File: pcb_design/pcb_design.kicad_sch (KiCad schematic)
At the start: 8 parts, among them J1 USB_C_Receptacle_USB2.0_16P, U1 AP2112K-3.3, U2 ESP32-C3-WROOM-02

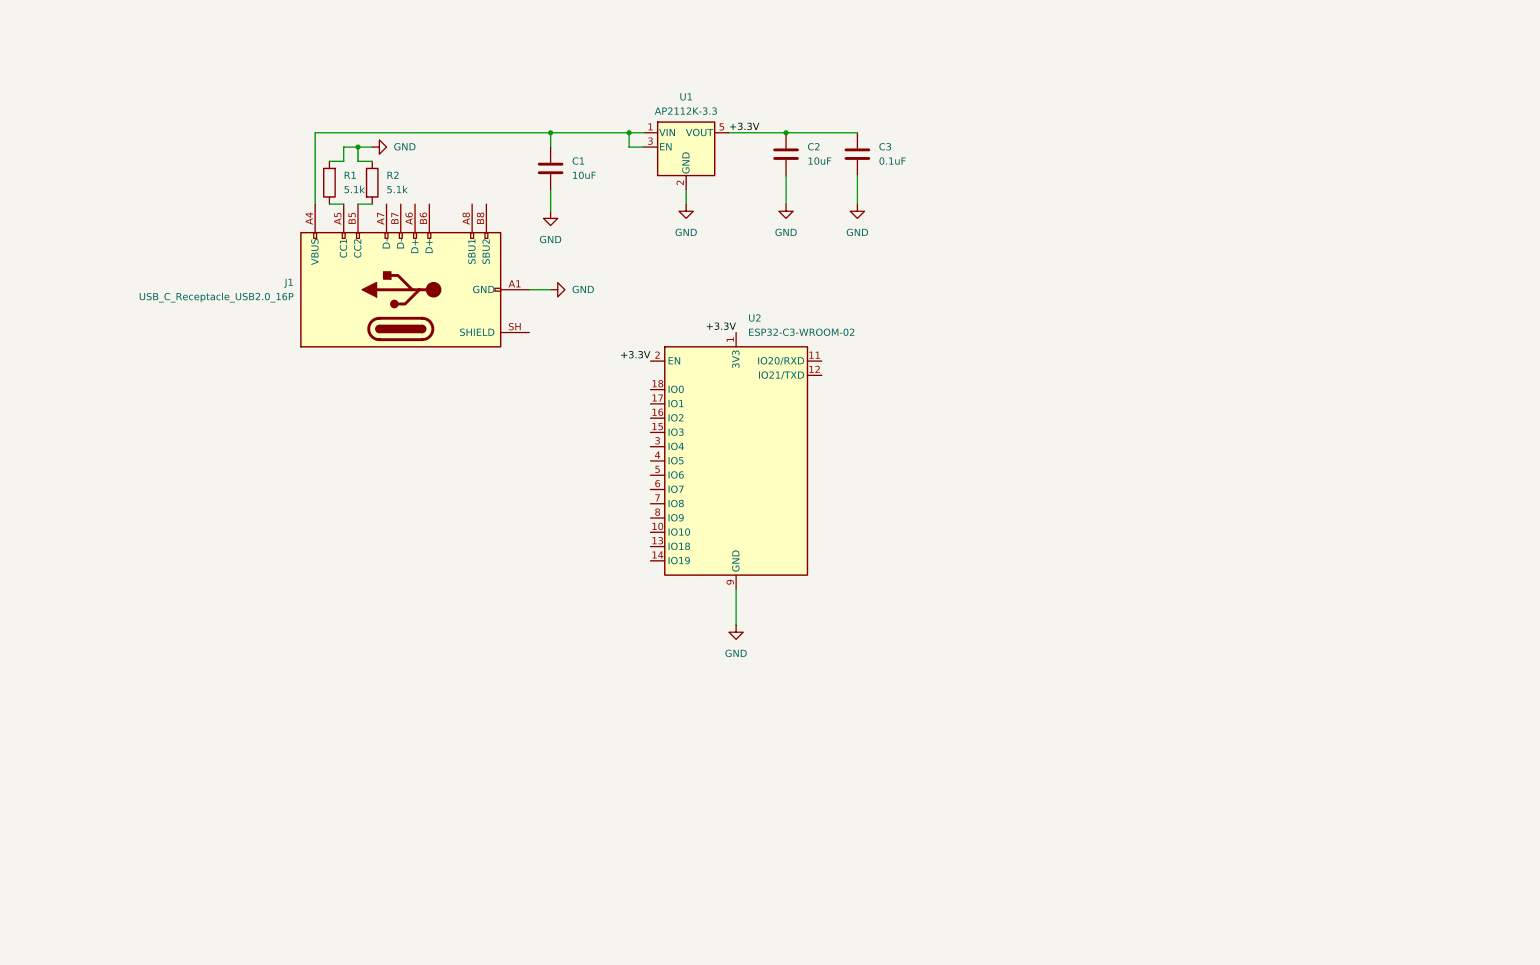
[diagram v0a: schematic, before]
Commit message: feat: completar esquema electronico de la pulsera con magnetometro real y carga LiPo
- Reemplaza el conector generico del QMC6308 por su simbolo/footprint real
  (WLCSP-4, libreria propia en pcb_design/libs) para ensamblaje SMT en JLCPCB
- Agrega regulador de 1.8V (AP2112K-1.8) y level shifter I2C (TXS0102DCU),
  porque el QMC6308 no soporta el bus de 3.3V ya existente
- Agrega circuito de carga LiPo (MCP73831) alimentado desde el mismo USB-C,
  con conector JST-PH para la bateria
- Reemplaza los transistores de simulacion por MMBT3904 reales y asigna
  footprint a todos los componentes (incluido el USB-C: HRO TYPE-C-31-M-12)
- Corrige la alimentacion del ESP32, los pull-ups I2C faltantes y la
  conexion CC1/CC2 del USB-C

Estructura de componentes, conexiones y revision asistida por Claude,
validado con ERC (0 errores) y verificacion de netlist en cada paso.

Co-Authored-By: Claude Sonnet 5 <noreply@anthropic.com>
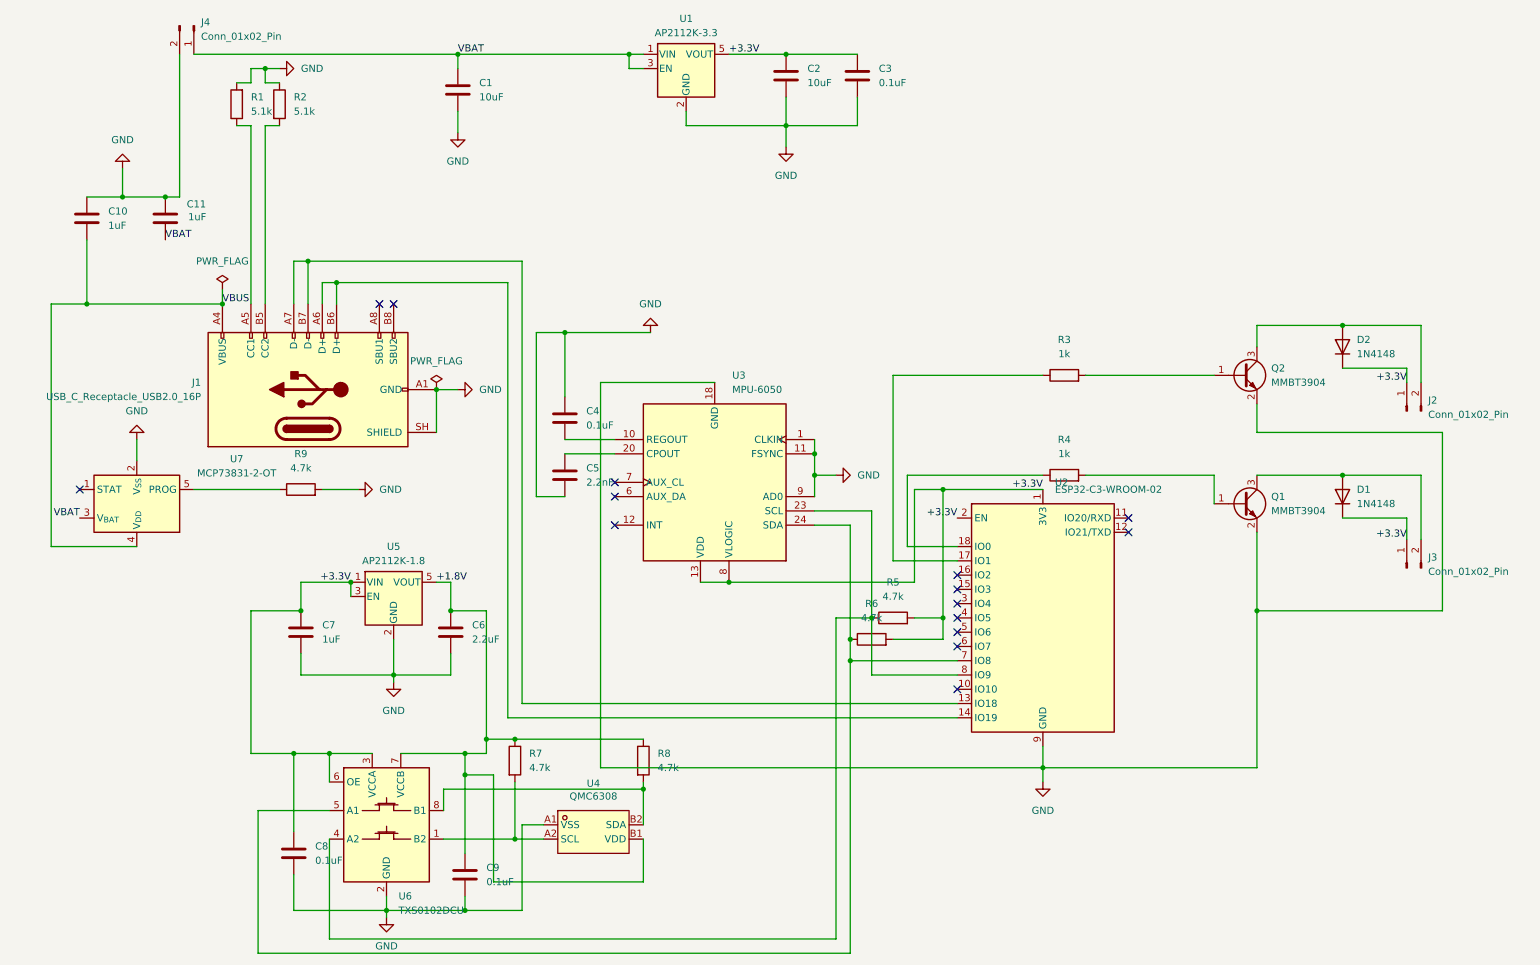
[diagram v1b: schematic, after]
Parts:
- added C10, C11: 1uF, Capacitor_SMD:C_0805_2012Metric, symbol Device:C
- added C4, C8, C9: 0.1uF, Capacitor_SMD:C_0603_1608Metric, symbol Device:C
- added C5: 2.2nF, Capacitor_SMD:C_0603_1608Metric, symbol Device:C
- added C6: 2.2uF, Capacitor_SMD:C_0805_2012Metric, symbol Device:C
- added C7: 1uF, Capacitor_SMD:C_0603_1608Metric, symbol Device:C
- added D1, D2: 1N4148, Diode_THT:D_DO-35_SOD27_P7.62mm_Horizontal, symbol Diode:1N4148
- added J2, J3: Conn_01x02_Pin, Connector_PinHeader_2.54mm:PinHeader_1x02_P2.54mm_Vertical, symbol Connector:Conn_01x02_Pin
- added J4: Conn_01x02_Pin, symbol Connector:Conn_01x02_Pin
- added Q1, Q2: MMBT3904, Package_TO_SOT_SMD:SOT-23, symbol Transistor_BJT:MMBT3904
- added R3, R4: 1k, Resistor_SMD:R_0603_1608Metric, symbol Device:R
- added R5, R6, R7, R8, R9: 4.7k, Resistor_SMD:R_0603_1608Metric, symbol Device:R
- added U3: MPU-6050, Sensor_Motion:InvenSense_QFN-24_4x4mm_P0.5mm, symbol Sensor_Motion:MPU-6050
- added U4: QMC6308, ACPI_QMC6308:WLCSP-4_L0.8-W0.8-R2-C2-P0.40-BL, symbol ACPI_QMC6308:QMC6308
- added U5: AP2112K-1.8, Package_TO_SOT_SMD:SOT-23-5, symbol Regulator_Linear:AP2112K-1.8
- added U6: TXS0102DCU, Package_SO:VSSOP-8_2.3x2mm_P0.5mm, symbol Logic_LevelTranslator:TXS0102DCU
- added U7: MCP73831-2-OT, Package_TO_SOT_SMD:SOT-23-5, symbol Battery_Management:MCP73831-2-OT
- C1, C2: footprint (none) -> Capacitor_SMD:C_0805_2012Metric
- C3: footprint (none) -> Capacitor_SMD:C_0603_1608Metric
- J1: footprint (none) -> Connector_USB:USB_C_Receptacle_HRO_TYPE-C-31-M-12
- R1, R2: footprint (none) -> Resistor_SMD:R_0603_1608Metric
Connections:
- net +3.3V: now also C7.1, C8.1, D1.1 (K), D2.1 (K), J2.1 (Pin_1), J3.1 (Pin_1), R5.2, R6.2, U3.13 (VDD), U3.8 (VLOGIC), U5.1 (VIN), U5.3 (EN), U6.3 (VCCA), U6.6 (OE)
- net GND: now also J1.SH (SHIELD), C10.1, C11.1, C4.2, C5.1, C6.2, C7.2, C8.2, C9.2, J4.2 (Pin_2), Q1.2 (E), Q2.2 (E), R9.2, U3.1 (CLKIN), U3.11 (FSYNC), U3.18 (GND), U3.9 (AD0), U4.A1 (VSS), U5.2 (GND), U6.2 (GND), U7.2 (V_{SS})
- net at U2.13 (IO18): now also J1.A7 (D-), J1.B7 (D-)
- net at U2.14 (IO19): now also J1.A6 (D+), J1.B6 (D+)
- net at U2.17 (IO1): now also R3.1
- net at U2.18 (IO0): now also R4.1
- net at U2.7 (IO8): now also R6.1, U3.24 (SDA), U6.5 (A1)
- net at U2.8 (IO9): now also R5.1, U3.23 (SCL), U6.4 (A2)
- net VBUS: now reaches J1.A4 (VBUS), J1.A9 (VBUS), J1.B4 (VBUS), J1.B9 (VBUS)
- net VBUS: now also C10.2, U7.4 (V_{DD}); no longer C1.1, U1.1 (VIN), U1.3 (EN)
- new net: C4.1, U3.10 (REGOUT)
- new net: C5.2, U3.20 (CPOUT)
- new net: R9.1, U7.5 (PROG)
- new net: D2.2 (A), J2.2 (Pin_2), Q2.3 (C)
- new net: D1.2 (A), J3.2 (Pin_2), Q1.3 (C)
- new net: Q2.1 (B), R3.2
- new net: R7.2, U4.A2 (SCL), U6.1 (B2)
- new net: R8.2, U4.B2 (SDA), U6.8 (B1)
- new net: Q1.1 (B), R4.2
- new net +1.8V: C6.1, C9.1, R7.1, R8.1, U4.B1 (VDD), U5.5 (VOUT), U6.7 (VCCB)
- new net VBAT: C1.1, C11.2, J4.1 (Pin_1), U1.1 (VIN), U1.3 (EN), U7.3 (V_{BAT})
- no-connect marks 0 -> 15
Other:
- moved on the sheet: C1, C2, C3, J1, R1, R2, U1, U2
